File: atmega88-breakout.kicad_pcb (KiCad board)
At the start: 2 copper layers, 10 parts, among them J1 Conn_01x08_Male, J2 ICSP Header, J4 Conn_01x08_Male, U1 ATmega88PA-AU

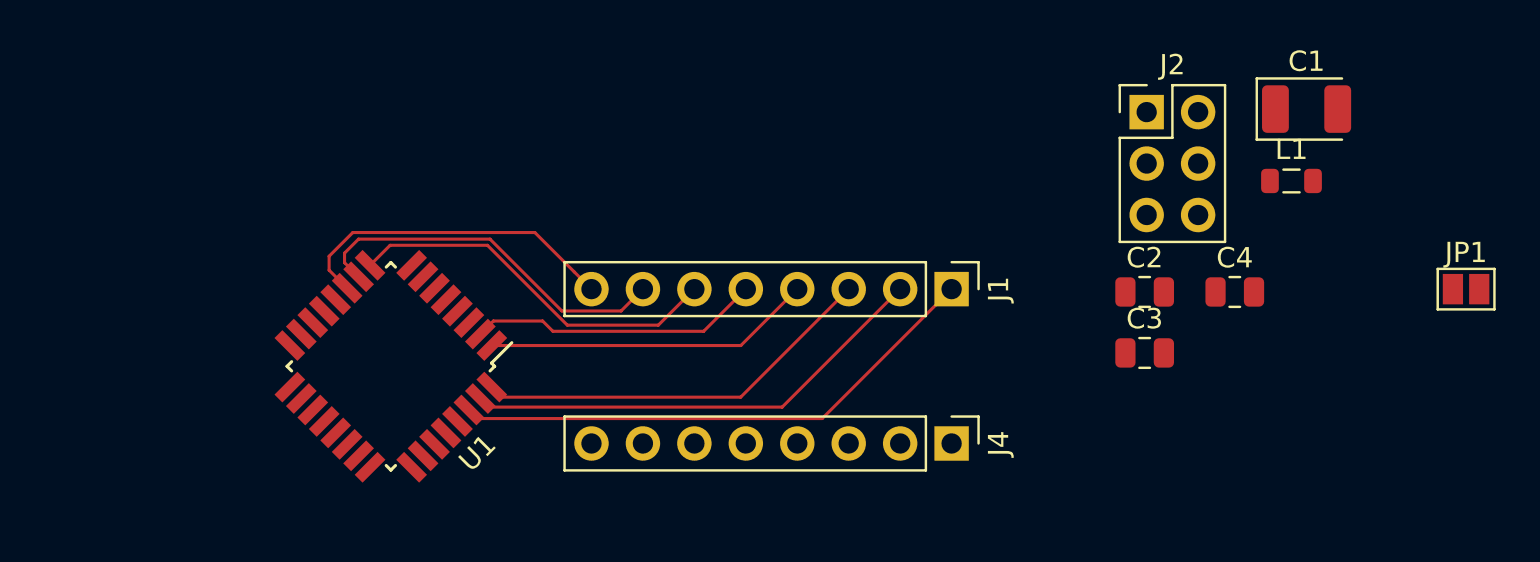
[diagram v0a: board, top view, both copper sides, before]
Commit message: Route all IO, add user LED, need to add power headers
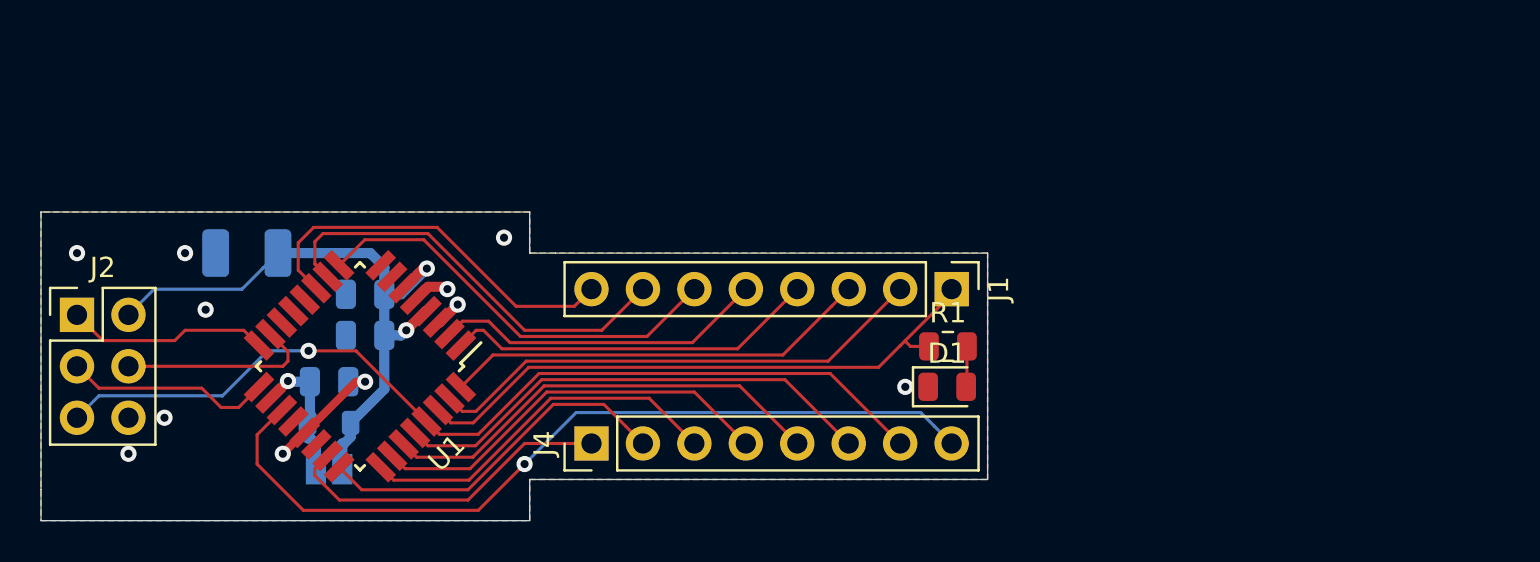
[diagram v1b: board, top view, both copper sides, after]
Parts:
- added D1: LED_Small, LED_SMD:LED_0805_2012Metric, F.Cu at (200.4, 68.3)
- added R1: R_Small, Resistor_SMD:R_0805_2012Metric, F.Cu at (200.5, 66.3)
- C1, C2, C3, C4, JP1, L1: moved to B.Cu
- moved JP1 56.8 mm to (169.9, 72.4), turned to 180 degrees
- moved J2 53.8 mm to (157.5, 64.8)
- moved C1 52.8 mm to (165.9, 61.7), turned to 180 degrees
- moved L1 49.0 mm to (169.9, 70.1), turned to 180 degrees
- moved C4 44.9 mm to (169.9, 68.1), turned to 180 degrees
- moved C3 38.5 mm to (171.7, 65.8)
- moved C2 38.5 mm to (171.7, 63.8)
- moved J4 17.8 mm to (182.9, 71.1), turned to 90 degrees
- moved U1 1.52 mm to (171.4, 67.3)
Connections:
- U1 pad 12: /B0 -> (no net)
- U1 pad 13: /B1 -> (no net)
- U1 pad 14: /B2 -> (no net)
- U1 pad 20: AREF -> (no net)
- U1 pad 22: ADC7 -> (no net)
- U1 pad 7: /B6 -> (no net)
- U1 pad 8: /B7 -> (no net)
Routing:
- net /C6: track 0.00 -> 46.4 mm, vias 0 -> 1
- net ADC6: track 0.00 -> 41.0 mm, vias 0 -> 1
- net VCC: track 0.00 -> 31.8 mm, vias 0 -> 2
- net /C5: track 0.00 -> 24.3 mm
- net /C4: track 0.00 -> 22.3 mm
- net /C3: track 0.00 -> 20.3 mm
- net /C2: track 0.00 -> 18.4 mm
- net /C1: track 0.00 -> 18.0 mm
- net /C0: track 0.00 -> 16.6 mm
- net /B5: track 0.00 -> 10.2 mm
- net /B4: track 0.00 -> 10.0 mm
- net /B3: track 0.00 -> 9.67 mm
- net GND: track 0.00 -> 9.61 mm, vias 0 -> 11
- net VAA: track 0.00 -> 6.93 mm, vias 0 -> 1
- net /D0: track 26.7 -> 29.8 mm
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- added copper zone on B.Cu, net GND
- added copper zone on F.Cu, net GND
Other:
- board outline added: 46.7 x 15.2 mm

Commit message: Rev A release (ordered)
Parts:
- removed J4: Conn_01x08_Male, Connector_PinHeader_2.54mm:PinHeader_1x08_P2.54mm_Vertical
- added B0: TestPoint, TestPoint:TestPoint_Pad_D1.5mm, B.Cu at (134.4, 102.6)
- added B1: TestPoint, TestPoint:TestPoint_Pad_D1.5mm, B.Cu at (130.3, 99.6)
- added B2: TestPoint, TestPoint:TestPoint_Pad_D1.5mm, B.Cu at (132.3, 104.9)
- added B3: TestPoint, TestPoint:TestPoint_Pad_D1.5mm, B.Cu at (127.5, 101.6)
- added B4: TestPoint, TestPoint:TestPoint_Pad_D1.5mm, B.Cu at (130.3, 106.4)
- added B5: TestPoint, TestPoint:TestPoint_Pad_D1.5mm, B.Cu at (128.0, 108.5)
- added B6: TestPoint, TestPoint:TestPoint_Pad_D1.5mm, B.Cu at (137.7, 99.3)
- added B7: TestPoint, TestPoint:TestPoint_Pad_D1.5mm, B.Cu at (134.4, 99.1)
- added J3: Conn_01x09, Connector_PinHeader_2.54mm:PinHeader_1x09_P2.54mm_Vertical, F.Cu at (145.8, 101.6)
- C1: footprint Capacitor_Tantalum_SMD:CP_EIA-3528-12_Kemet-T -> Capacitor_Tantalum_SMD:CP_EIA-3216-18_Kemet-A; moved to F.Cu
- C2, C3, C4, L1: moved to F.Cu
- J1: value Conn_01x08_Male -> Conn_01x09; footprint Connector_PinHeader_2.54mm:PinHeader_1x08_P2.54mm_Vertical -> Connector_PinHeader_2.54mm:PinHeader_1x09_P2.54mm_Vertical
- R1: value R_Small -> 1k
- moved J1 71.4 mm to (145.8, 109.2), turned to 90 degrees
- moved L1 59.1 mm to (127.3, 111.0), turned to 0 degrees
- moved C4 59.1 mm to (127.3, 109.0), turned to 0 degrees
- moved C1 58.2 mm to (121.7, 99.6)
- moved JP1 57.4 mm to (127.4, 111.0), turned to 0 degrees
- moved D1 53.2 mm to (163.4, 106.4)
- moved ICSP 53.2 mm to (120.4, 102.9)
- moved R1 53.2 mm to (163.4, 104.4)
- moved U1 53.2 mm to (134.4, 105.4)
- moved C2 49.5 mm to (139.2, 101.1), turned to 135 degrees
- moved C3 40.0 mm to (166.1, 105.3), turned to 90 degrees
- renumbered J2 to ICSP
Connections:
- J1 pad 1: /D0 -> ADC6
- J1 pad 2: /D1 -> /C0
- J1 pad 3: /D2 -> /C1
- J1 pad 4: /D3 -> /C2
- J1 pad 5: /D4 -> /C3
- J1 pad 6: /D5 -> /C4
- J1 pad 7: /D6 -> /C5
- J1 pad 8: /D7 -> /C6
- U1 pad 12: (no net) -> /B0
- U1 pad 13: (no net) -> /B1
- U1 pad 14: (no net) -> /B2
- U1 pad 20: (no net) -> VAA
- U1 pad 22: (no net) -> ADC7
- U1 pad 7: (no net) -> /B6
- U1 pad 8: (no net) -> /B7
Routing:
- net VCC: track 31.8 -> 70.2 mm
- net ADC6: track 41.0 -> 21.2 mm, vias 1 -> 0
- net /B5: track 10.2 -> 17.4 mm, vias 0 -> 1
- net /B4: track 10.0 -> 16.7 mm, vias 0 -> 1
- net VAA: track 6.93 -> 11.3 mm
- net /C0: track 16.6 -> 20.6 mm
- net /B1: track 0.00 -> 3.65 mm, vias 0 -> 1
- net /B0: track 0.00 -> 3.35 mm, vias 0 -> 1
- net /C6: track 46.4 -> 49.7 mm, vias 1 -> 0
- net /B2: track 0.00 -> 2.55 mm, vias 0 -> 1
- net /C5: track 24.3 -> 26.9 mm
- net /C4: track 22.3 -> 24.8 mm
- net /B6: track 0.00 -> 2.45 mm, vias 0 -> 1
- net /C3: track 20.3 -> 22.7 mm
- net /C2: track 18.4 -> 20.6 mm
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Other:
- board size 46.7 x 15.2 mm -> 49.4 x 15.2 mm
- board text added: "AD6 C0 C1 C2 C3 C4 C5 ~R~ GND"
- board text added: "D7 D6 D5 D4 D3 D2 D1 D0 VCC"
